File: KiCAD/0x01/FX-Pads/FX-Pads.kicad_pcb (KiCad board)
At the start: 2 copper layers, 100 x 100 mm, 56 parts, among them J1 CONTROL, J2 DATA, SW1 SW_Push, SW10 SW_Push, SW11 SW_Push, SW12 SW_Push, SW13 SW_Push, SW14 SW_Push, SW15 SW_Push, SW16 SW_Push, SW2 SW_Push, SW3 SW_Push, SW4 SW_Push, SW5 SW_Push, SW6 SW_Push, SW7 SW_Push, SW8 SW_Push, SW9 SW_Push, U1 CD74HC4067M

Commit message: fx-pads routing
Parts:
- removed J2: DATA, Connector_PinHeader_2.54mm:PinHeader_1x04_P2.54mm_Vertical
- added C1: 10uF, Capacitor_SMD:C_0805_2012Metric_Pad1.18x1.45mm_HandSolder, F.Cu at (106.0, 98.5)
- added D12: 1N4148, Diode_SMD:D_SOD-123, B.Cu at (55.0, 70.0)
- added D13: 1N4148, Diode_SMD:D_SOD-123, B.Cu at (80.0, 71.0)
- added D14: 1N4148, Diode_SMD:D_SOD-123, B.Cu at (104.0, 68.0)
- added D15: 1N4148, Diode_SMD:D_SOD-123, B.Cu at (129.0, 71.0)
- added D16: 1N4148, Diode_SMD:D_SOD-123, B.Cu at (55.0, 96.0)
- added D17: 1N4148, Diode_SMD:D_SOD-123, B.Cu at (80.0, 97.0)
- added D18: 1N4148, Diode_SMD:D_SOD-123, B.Cu at (103.0, 83.0)
- added D19: 1N4148, Diode_SMD:D_SOD-123, B.Cu at (129.0, 95.0)
- added D22: 1N4148, Diode_SMD:D_SOD-123, B.Cu at (105.0, 109.0)
- added D27: 1N4148, Diode_SMD:D_SOD-123, B.Cu at (55.0, 120.0)
- added D28: 1N4148, Diode_SMD:D_SOD-123, B.Cu at (104.0, 120.0)
- added D29: 1N4148, Diode_SMD:D_SOD-123, B.Cu at (129.0, 120.0)
- added D30: 1N4148, Diode_SMD:D_SOD-123, B.Cu at (55.0, 130.0)
- added D31: 1N4148, Diode_SMD:D_SOD-123, B.Cu at (96.0, 83.0)
- added D32: 1N4148, Diode_SMD:D_SOD-123, B.Cu at (78.0, 129.0)
- added D33: 1N4148, Diode_SMD:D_SOD-123, B.Cu at (105.0, 128.0)
- added D34: 1N4148, Diode_SMD:D_SOD-123, B.Cu at (129.0, 129.0)
- added D35: 1N4148, Diode_SMD:D_SOD-123, B.Cu at (102.0, 109.0)
- added D9: 1N4148, Diode_SMD:D_SOD-323_HandSoldering, F.Cu at (111.0, 100.0)
- added JP1: A0, Jumper:SolderJumper-2_P1.3mm_Open_RoundedPad1.0x1.5mm, F.Cu at (121.0, 102.0)
- added JP2: A1, Jumper:SolderJumper-2_P1.3mm_Open_RoundedPad1.0x1.5mm, F.Cu at (121.0, 98.5)
- added R2: 47K, Resistor_SMD:R_0805_2012Metric_Pad1.20x1.40mm_HandSolder, F.Cu at (116.5, 102.0)
- added R3: 47K, Resistor_SMD:R_0805_2012Metric_Pad1.20x1.40mm_HandSolder, F.Cu at (116.5, 98.5)
- added R4: 10K, Resistor_SMD:R_0805_2012Metric_Pad1.20x1.40mm_HandSolder, B.Cu at (106.0, 91.0)
- added R5: 10K, Resistor_SMD:R_0805_2012Metric_Pad1.20x1.40mm_HandSolder, B.Cu at (102.5, 91.0)
- J1: value CONTROL -> Conn_01x05; footprint Connector_PinHeader_2.54mm:PinHeader_1x04_P2.54mm_Vertical -> Connector_JST:JST_PH_S5B-PH-K_1x05_P2.00mm_Horizontal
- U1: value CD74HC4067M -> HT16K33 24SOP
- moved D10 75.0 mm to (137.5, 87.5)
- moved D2 75.0 mm to (62.5, 137.5)
- moved D25 75.0 mm to (62.5, 87.5)
- moved D8 75.0 mm to (137.5, 137.5)
- moved D20 25.0 mm to (112.5, 87.5)
- moved D23 25.0 mm to (87.5, 87.5)
- moved D4 25.0 mm to (87.5, 137.5)
- moved D6 25.0 mm to (112.5, 137.5)
- moved U1 12.5 mm to (100.0, 100.0)
- moved J1 8.18 mm to (96.0, 77.5), turned to 0 degrees
- renumbered D5 to D10, D12 to D11, D16 to D2, D6 to D20, D11 to D21, D7 to D23, D10 to D24, D8 to D25, D9 to D26, D2 to D3, D15 to D4, D3 to D5, D14 to D6, D4 to D7, D13 to D8, H3 to H1, H4 to H2, H1 to H3, H2 to H4
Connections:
- D1 pad 1: VCC -> +5V
- D10 pad 1: VCC -> +5V
- D11 pad 1: VCC -> +5V
- D2 pad 1: VCC -> +5V
- D20 pad 1: VCC -> +5V
- D21 pad 1: VCC -> +5V
- D23 pad 1: VCC -> +5V
- D24 pad 1: VCC -> +5V
- D25 pad 1: VCC -> +5V
- D26 pad 1: VCC -> +5V
- D3 pad 1: VCC -> +5V
- D4 pad 1: VCC -> +5V
- D5 pad 1: VCC -> +5V
- D6 pad 1: VCC -> +5V
- D7 pad 1: VCC -> +5V
- D8 pad 1: VCC -> +5V
- J1 pad 1: /S0 -> GND
- J1 pad 2: /S1 -> +5V
- J1 pad 3: /S2 -> /SDA
- J1 pad 4: /S3 -> /SCL
- SW1 pad 1: Net-(U1-I0) -> Net-(D12-A)
- SW1 pad 2: GND -> Net-(D22-K)
- SW10 pad 1: Net-(U1-I9) -> Net-(D28-A)
- SW10 pad 2: GND -> Net-(D35-K)
- SW11 pad 1: Net-(U1-I10) -> Net-(D29-A)
- SW11 pad 2: GND -> Net-(D35-K)
- SW12 pad 1: Net-(U1-I11) -> Net-(D30-A)
- SW12 pad 2: GND -> Net-(D35-K)
- SW13 pad 1: Net-(U1-I12) -> Net-(D31-A)
- SW13 pad 2: GND -> Net-(D35-K)
- SW14 pad 1: Net-(U1-I13) -> Net-(D32-A)
- SW14 pad 2: GND -> Net-(D35-K)
- SW15 pad 1: Net-(U1-I14) -> Net-(D33-A)
- SW15 pad 2: GND -> Net-(D35-K)
- SW16 pad 1: Net-(U1-I15) -> Net-(D34-A)
- SW16 pad 2: GND -> Net-(D35-K)
- SW2 pad 1: Net-(U1-I1) -> Net-(D13-A)
- SW2 pad 2: GND -> Net-(D22-K)
- SW3 pad 1: Net-(U1-I2) -> Net-(D14-A)
- SW3 pad 2: GND -> Net-(D22-K)
- SW4 pad 1: Net-(U1-I3) -> Net-(D15-A)
- SW4 pad 2: GND -> Net-(D22-K)
- SW5 pad 1: Net-(U1-I4) -> Net-(D16-A)
- SW5 pad 2: GND -> Net-(D22-K)
- SW6 pad 1: Net-(U1-I5) -> Net-(D17-A)
- SW6 pad 2: GND -> Net-(D22-K)
- SW7 pad 1: Net-(U1-I6) -> Net-(D18-A)
- SW7 pad 2: GND -> Net-(D22-K)
- SW8 pad 1: Net-(U1-I7) -> Net-(D19-A)
- SW8 pad 2: GND -> Net-(D22-K)
- SW9 pad 1: Net-(U1-I8) -> Net-(D27-A)
- SW9 pad 2: GND -> Net-(D35-K)
- U1 pad 1: /OUT -> GND
- U1 pad 10: /S0 -> unconnected-(U1-ROW11/K10/INT-Pad10)
- U1 pad 11: /S1 -> unconnected-(U1-ROW10/K9-Pad11)
- U1 pad 12: GND -> /R9
- U1 pad 13: /S3 -> /R8
- U1 pad 14: /S2 -> /R7
- U1 pad 15: GND -> /R6
- U1 pad 16: Net-(U1-I15) -> /R5
- U1 pad 17: Net-(U1-I14) -> /R4
- U1 pad 18: Net-(U1-I13) -> /R3
- U1 pad 19: Net-(U1-I12) -> /R2
- U1 pad 2: Net-(U1-I7) -> /COM0
- U1 pad 20: Net-(U1-I11) -> /A0
- U1 pad 21: Net-(U1-I10) -> /A1
- U1 pad 22: Net-(U1-I9) -> /SCL
- U1 pad 23: Net-(U1-I8) -> /SDA
- U1 pad 24: VCC -> +5V
- U1 pad 3: Net-(U1-I6) -> /COM1
- U1 pad 4: Net-(U1-I5) -> /COM2
- U1 pad 5: Net-(U1-I4) -> unconnected-(U1-COM3/KS2-Pad5)
- U1 pad 6: Net-(U1-I3) -> unconnected-(U1-COM4-Pad6)
- U1 pad 7: Net-(U1-I2) -> unconnected-(U1-COM5-Pad7)
- U1 pad 8: Net-(U1-I1) -> unconnected-(U1-COM6-Pad8)
- U1 pad 9: Net-(U1-I0) -> unconnected-(U1-COM7-Pad9)
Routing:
- net VCC: track 457.4 -> 0.00 mm, vias 27 -> 0
- net GND: track 240.2 -> 0.00 mm, vias 36 -> 0
- net Net-(U1-I11): track 178.3 -> 0.00 mm, vias 1 -> 0
- net Net-(U1-I13): track 158.0 -> 0.00 mm, vias 1 -> 0
- net Net-(U1-I2): track 145.0 -> 0.00 mm, vias 3 -> 0
- net Net-(U1-I3): track 141.7 -> 0.00 mm, vias 1 -> 0
- net Net-(U1-I14): track 137.7 -> 0.00 mm, vias 1 -> 0
- net /OUT: track 127.5 -> 0.00 mm, vias 4 -> 0
- net Net-(U1-I15): track 115.8 -> 0.00 mm, vias 1 -> 0
- net /S1: track 105.3 -> 0.00 mm, vias 4 -> 0
- net Net-(U1-I0): track 104.1 -> 0.00 mm, vias 1 -> 0
- net Net-(U1-I1): track 96.3 -> 0.00 mm, vias 5 -> 0
- net Net-(U1-I4): track 84.3 -> 0.00 mm, vias 3 -> 0
- net Net-(U1-I7): track 67.8 -> 0.00 mm, vias 1 -> 0
- net Net-(D25-DOUT): track 91.4 -> 25.0 mm, vias 4 -> 2
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- added copper zone on B.Cu, net +5V
- removed copper zone on B.Cu, net VCC

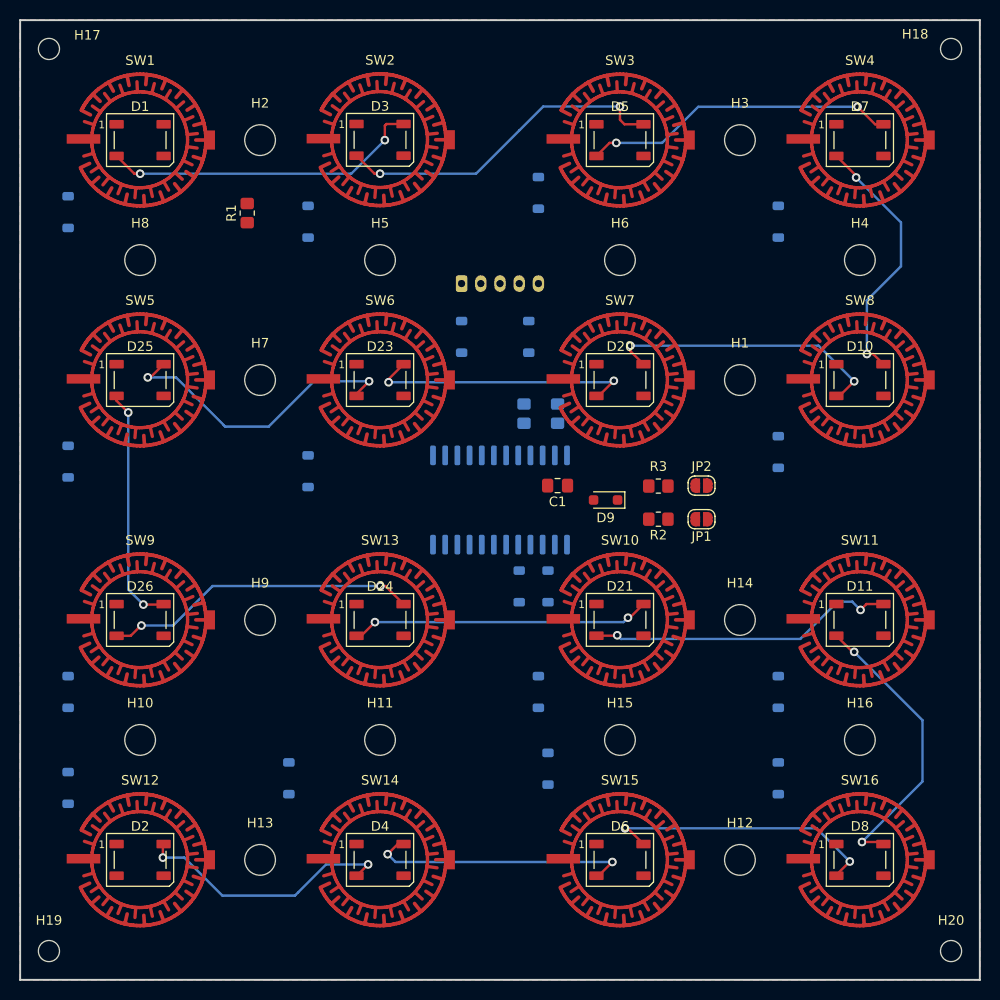
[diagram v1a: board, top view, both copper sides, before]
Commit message: pads routing
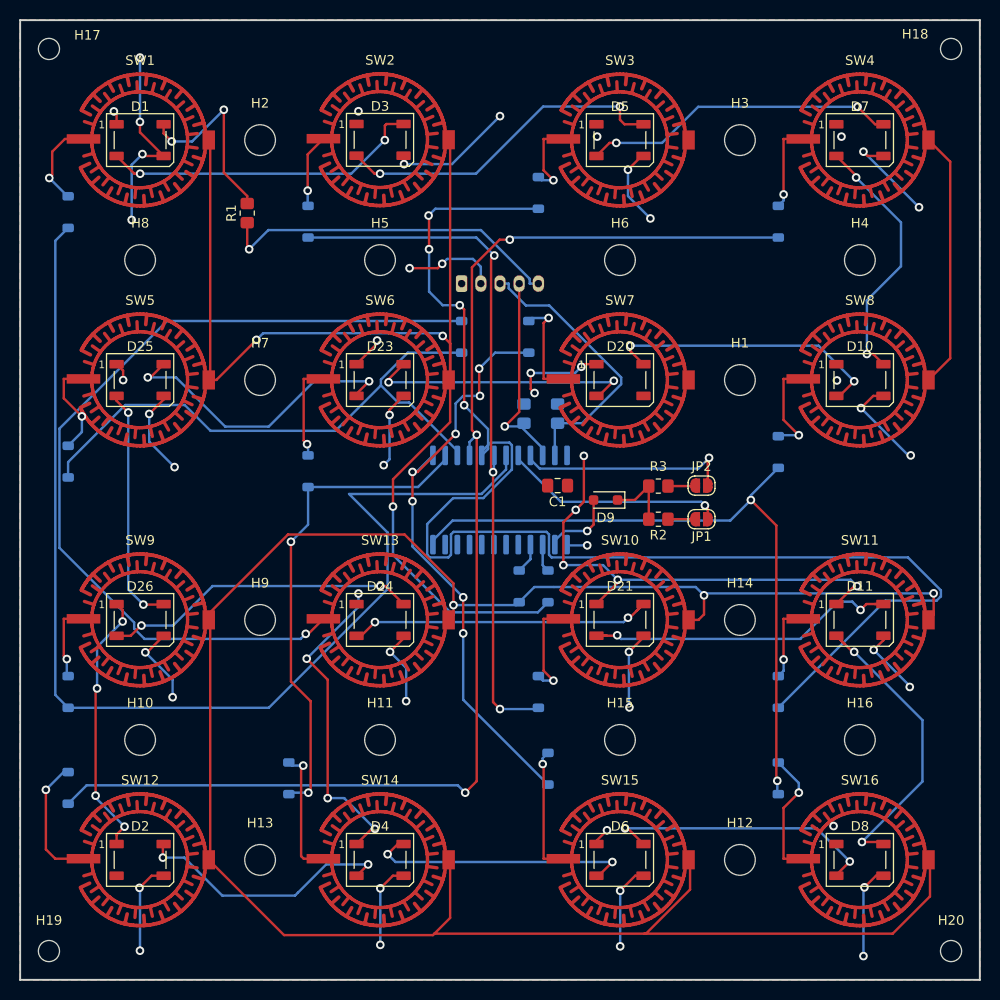
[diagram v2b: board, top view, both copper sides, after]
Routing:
- net Net-(D35-K): track 0.00 -> 221.1 mm, vias 0 -> 3
- net GND: track 0.00 -> 151.0 mm, vias 0 -> 33
- net Net-(D22-K): track 0.00 -> 148.2 mm, vias 0 -> 3
- net /R4: track 0.00 -> 143.7 mm, vias 0 -> 4
- net +5V: track 0.00 -> 139.6 mm, vias 0 -> 27
- net /R5: track 0.00 -> 133.6 mm, vias 0 -> 3
- net /R2: track 0.00 -> 120.0 mm
- net Net-(D31-A): track 0.00 -> 91.6 mm, vias 0 -> 1
- net /R3: track 0.00 -> 73.8 mm, vias 0 -> 3
- net /R9: track 0.00 -> 71.7 mm, vias 0 -> 2
- net /R8: track 0.00 -> 62.2 mm, vias 0 -> 7
- net /R6: track 0.00 -> 61.2 mm
- net /R7: track 0.00 -> 51.6 mm, vias 0 -> 2
- net /NP_DATA: track 0.00 -> 36.4 mm, vias 0 -> 1
- net /SDA: track 0.00 -> 29.4 mm
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
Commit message: micropython
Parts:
- added C2: 1uF, Capacitor_SMD:C_0603_1608Metric_Pad1.08x0.95mm_HandSolder, B.Cu at (112.3, 57.5)
- added C3: 1uF, Capacitor_SMD:C_0603_1608Metric_Pad1.08x0.95mm_HandSolder, B.Cu at (137.4, 82.5)
- added C4: 1uF, Capacitor_SMD:C_0603_1608Metric_Pad1.08x0.95mm_HandSolder, B.Cu at (87.4, 83.4)
- added C5: 1uF, Capacitor_SMD:C_0603_1608Metric_Pad1.08x0.95mm_HandSolder, B.Cu at (62.4, 107.5)
- added C6: 1uF, Capacitor_SMD:C_0603_1608Metric_Pad1.08x0.95mm_HandSolder, B.Cu at (112.6, 107.5)
- added C7: 1uF, Capacitor_SMD:C_0603_1608Metric_Pad1.08x0.95mm_HandSolder, B.Cu at (137.4, 132.5)
- added C8: 1uF, Capacitor_SMD:C_0603_1608Metric_Pad1.08x0.95mm_HandSolder, B.Cu at (87.2, 131.9)
- added C9: 1uF, Capacitor_SMD:C_0603_1608Metric_Pad1.08x0.95mm_HandSolder, B.Cu at (62.6, 57.5)
- D28: renamed from D14; moved to F.Cu
- D9: footprint Diode_SMD:D_SOD-323_HandSoldering -> Diode_SMD:D_SOD-123
- moved D22 28.4 mm to (79.4, 106.0), turned to -90 degrees
- moved R4 14.1 mm to (100.3, 78.1), turned to 90 degrees
- moved R5 12.9 mm to (102.5, 78.1), turned to 90 degrees
- moved D28 4.74 mm to (101.1, 64.3)
- moved J1 3.67 mm to (96.6, 73.8)
- moved D21 2.16 mm to (53.8, 131.8), turned to -90 degrees
- moved C1 2.00 mm to (104.8, 100.1)
- moved D32 1.93 mm to (102.1, 84.7)
- moved D18 1.76 mm to (54.4, 118.4)
- moved D9 0.76 mm to (111.8, 100.1)
- turned D23 to -90 degrees
- turned D24 to -90 degrees
- turned D25 to -90 degrees
- renumbered D20 to D12, D21 to D13, D23 to D14, D24 to D15, D25 to D16, D26 to D17, D27 to D18, D28 to D19, D29 to D20, D30 to D21, D31 to D22, D32 to D23, D33 to D24, D34 to D25, D12 to D26, D13 to D27, D15 to D29, D16 to D30, D17 to D31, D18 to D32, D19 to D33, D35 to D34, D22 to D35, SW9 to SW1, SW2 to SW10, SW3 to SW11, SW4 to SW12, SW5 to SW13, SW6 to SW14, SW7 to SW15, SW8 to SW16, SW10 to SW2, SW11 to SW3, SW12 to SW4, SW13 to SW5, SW14 to SW6, SW15 to SW7, SW16 to SW8, SW1 to SW9
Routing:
- net +5V: track 139.6 -> 482.1 mm, vias 27 -> 33
- net GND: track 151.0 -> 436.3 mm, vias 33 -> 37
- net Net-(D35-K): track 148.2 -> 294.7 mm, vias 3 -> 1
- net Net-(D22-A): track 91.6 -> 6.17 mm
- net /R4: track 143.7 -> 93.0 mm, vias 4 -> 7
- net /R8: track 62.2 -> 91.5 mm, vias 7 -> 8
- net /R9: track 71.7 -> 95.3 mm, vias 2 -> 4
- net Net-(D34-K): track 221.1 -> 240.3 mm, vias 3 -> 2
- net /R5: track 133.6 -> 122.2 mm, vias 3 -> 8
- net /A0: track 23.4 -> 31.6 mm
- net /R6: track 61.2 -> 53.0 mm, vias 0 -> 2
- net Net-(D21-A): track 13.6 -> 5.63 mm
- net Net-(D10-DIN): track 27.1 -> 34.9 mm
- net /R3: track 73.8 -> 80.7 mm, vias 3 -> 4
- net Net-(D1-DIN): track 19.7 -> 14.1 mm
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- added copper zone on B.Cu, net GND
- removed copper zone on B.Cu, net +5V
